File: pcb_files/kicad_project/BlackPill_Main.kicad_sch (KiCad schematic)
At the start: 32 parts, among them J10 Conn_01x04_Pin, J11 Conn_01x05_Pin, J9 Conn_01x04_Pin

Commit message: Actualiza el esquemático de la PCB
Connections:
- net BTN_MENU_MODE: now also U?.17 (B9); no longer U?.9 (A12)
- net BTN_START: now also U?.16 (B8); no longer U?.8 (A11)
- net LED_4: now also U?.24 (B10); no longer U?.5 (A8)
- net LED_5: now also U?.5 (A8); no longer U?.2 (B13)
- net LED_6: now also U?.26 (B1); no longer U?.1 (B12)
- net SPI_SCK: now also U?.2 (B13); no longer U?.24 (B10)
- net USART_RX renamed USART1_RX
- net USART_TX renamed USART1_TX
- new net SPI_NSS: U?.1 (B12)
- new net USART6_RX: U?.9 (A12)
- new net USART6_TX: U?.8 (A11)
- no-connect marks 14 -> 11
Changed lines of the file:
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@@
   (no_connect (at 80.01 185.42))
   (no_connect (at 97.79 81.28))
-  (no_connect (at 129.54 50.8))
   (no_connect (at 129.54 38.1))
   (no_connect (at 80.01 187.96))
   (no_connect (at 27.94 179.07))
-  (no_connect (at 97.79 76.2))
   (no_connect (at 80.01 168.91))
   (no_connect (at 129.54 53.34))
-  (no_connect (at 97.79 78.74))
   (no_connect (at 45.72 184.15))
   (no_connect (at 129.54 86.36))
@@
     (stroke (width 0) (type default))
   )
+  (wire (pts (xy 77.47 76.2) (xy 97.79 76.2))
+    (stroke (width 0) (type default))
+  )
   (wire (pts (xy 46.99 67.31) (xy 27.94 67.31))
     (stroke (width 0) (type default))
@@
     (stroke (width 0) (type default))
   )
-  (wire (pts (xy 144.78 48.26) (xy 129.54 48.26))
+  (wire (pts (xy 138.43 48.26) (xy 129.54 48.26))
     (stroke (width 0) (type default))
   )
@@
     (stroke (width 0) (type default))
   )
+  (wire (pts (xy 138.43 45.72) (xy 129.54 45.72))
+    (stroke (width 0) (type default))
+  )
   (wire (pts (xy 129.54 73.66) (xy 142.24 73.66))
     (stroke (width 0) (type default))
@@
     (stroke (width 0) (type default))
   )
-  (wire (pts (xy 81.28 38.1) (xy 97.79 38.1))
-    (stroke (width 0) (type default))
-  )
   (wire (pts (xy 270.51 107.95) (xy 267.97 107.95))
     (stroke (width 0) (type default))
@@
     (stroke (width 0) (type default))
   )
+  (wire (pts (xy 138.43 50.8) (xy 129.54 50.8))
+    (stroke (width 0) (type default))
+  )
   (wire (pts (xy 115.57 90.17) (xy 115.57 100.33))
     (stroke (width 0) (type default))
@@
     (stroke (width 0) (type default))
   )
-  (wire (pts (xy 153.67 40.64) (xy 129.54 40.64))
+  (wire (pts (xy 147.32 40.64) (xy 129.54 40.64))
     (stroke (width 0) (type default))
   )
@@
     (stroke (width 0) (type default))
   )
-  (wire (pts (xy 149.86 43.18) (xy 129.54 43.18))
-    (stroke (width 0) (type default))
-  )
-  (wire (pts (xy 81.28 55.88) (xy 97.79 55.88))
+  (wire (pts (xy 143.51 43.18) (xy 129.54 43.18))
     (stroke (width 0) (type default))
   )
@@
     (stroke (width 0) (type default))
   )
+  (wire (pts (xy 77.47 78.74) (xy 97.79 78.74))
+    (stroke (width 0) (type default))
+  )
   (wire (pts (xy 270.51 43.18) (xy 267.97 43.18))
     (stroke (width 0) (type default))
@@
     (stroke (width 0) (type default))
   )
-  (wire (pts (xy 81.28 40.64) (xy 97.79 40.64))
-    (stroke (width 0) (type default))
-  )
-  (wire (pts (xy 81.28 58.42) (xy 97.79 58.42))
-    (stroke (width 0) (type default))
+  (label "BTN_MENU_MODE" (at 77.47 78.74 0) (fields_autoplaced)
+    (effects (font (size 1.27 1.27)) (justify left bottom))
   )
   (label "LED_4" (at 254 82.55 0) (fields_autoplaced)
@@
     (effects (font (size 1.27 1.27)) (justify left bottom))
   )
-  (label "LED_3" (at 144.78 48.26 180) (fields_autoplaced)
+  (label "LED_3" (at 138.43 48.26 180) (fields_autoplaced)
     (effects (font (size 1.27 1.27)) (justify right bottom))
   )
@@
     (effects (font (size 1.27 1.27)) (justify right bottom))
   )
-  (label "USART_TX" (at 81.28 50.8 0) (fields_autoplaced)
+  (label "USART1_TX" (at 81.28 50.8 0) (fields_autoplaced)
     (effects (font (size 1.27 1.27)) (justify left bottom))
   )
@@
     (effects (font (size 1.524 1.524)) (justify left bottom))
   )
-  (label "BTN_START" (at 81.28 55.88 0) (fields_autoplaced)
+  (label "BTN_START" (at 77.47 76.2 0) (fields_autoplaced)
     (effects (font (size 1.27 1.27)) (justify left bottom))
   )
@@
     (effects (font (size 1.27 1.27)) (justify left bottom))
   )
+  (label "LED_6" (at 138.43 50.8 180) (fields_autoplaced)
+    (effects (font (size 1.27 1.27)) (justify right bottom))
+  )
   (label "SWCLK" (at 115.57 100.33 90) (fields_autoplaced)
     (effects (font (size 1.524 1.524)) (justify left bottom))
@@
     (effects (font (size 1.27 1.27)) (justify right bottom))
   )
-  (label "USART_RX" (at 128.27 113.03 0) (fields_autoplaced)
+  (label "USART1_RX" (at 128.27 113.03 0) (fields_autoplaced)
     (effects (font (size 1.27 1.27)) (justify left bottom))
   )
-  (label "LED_6" (at 81.28 38.1 0) (fields_autoplaced)
+  (label "USART1_TX" (at 128.27 110.49 0) (fields_autoplaced)
     (effects (font (size 1.27 1.27)) (justify left bottom))
   )
-  (label "USART_TX" (at 128.27 110.49 0) (fields_autoplaced)
+  (label "USART1_RX" (at 81.28 53.34 0) (fields_autoplaced)
     (effects (font (size 1.27 1.27)) (justify left bottom))
   )
-  (label "USART_RX" (at 81.28 53.34 0) (fields_autoplaced)
-    (effects (font (size 1.27 1.27)) (justify left bottom))
-  )
   (label "SENSOR_1" (at 142.24 73.66 180) (fields_autoplaced)
     (effects (font (size 1.27 1.27)) (justify right bottom))
@@
   )
   (label "BTN_MENU_MODE" (at 240.03 52.07 180) (fields_autoplaced)
+    (effects (font (size 1.27 1.27)) (justify right bottom))
+  )
+  (label "LED_4" (at 138.43 45.72 180) (fields_autoplaced)
     (effects (font (size 1.27 1.27)) (justify right bottom))
   )
@@
     (effects (font (size 1.27 1.27)) (justify right bottom))
   )
-  (label "LED_5" (at 81.28 40.64 0) (fields_autoplaced)
-    (effects (font (size 1.27 1.27)) (justify left bottom))
-  )
   (label "SENSOR_3" (at 142.24 68.58 180) (fields_autoplaced)
     (effects (font (size 1.27 1.27)) (justify right bottom))
-  )
-  (label "BTN_MENU_MODE" (at 81.28 58.42 0) (fields_autoplaced)
-    (effects (font (size 1.27 1.27)) (justify left bottom))
   )
   (label "LED_2" (at 254 55.88 0) (fields_autoplaced)
@@
     (effects (font (size 1.27 1.27)) (justify right bottom))
   )
-  (label "LED_4" (at 81.28 48.26 0) (fields_autoplaced)
+  (label "LED_5" (at 81.28 48.26 0) (fields_autoplaced)
     (effects (font (size 1.27 1.27)) (justify left bottom))
   )
@@
     (effects (font (size 1.27 1.27)) (justify right))
   )
+  (hierarchical_label "SPI_SCK" (shape bidirectional) (at 97.79 40.64 180) (fields_autoplaced)
+    (effects (font (size 1.27 1.27)) (justify right))
+  )
   (hierarchical_label "ENC_2_I" (shape input) (at 97.79 60.96 180) (fields_autoplaced)
     (effects (font (size 1.27 1.27)) (justify right))
@@
     (effects (font (size 1.27 1.27)) (justify right))
   )
+  (hierarchical_label "USART6_TX" (shape input) (at 97.79 55.88 180) (fields_autoplaced)
+    (effects (font (size 1.27 1.27)) (justify right))
+  )
   (hierarchical_label "ENC_2_B" (shape input) (at 97.79 66.04 180) (fields_autoplaced)
     (effects (font (size 1.27 1.27)) (justify right))
@@
     (effects (font (size 1.27 1.27)) (justify right))
   )
+  (hierarchical_label "SPI_NSS" (shape bidirectional) (at 97.79 38.1 180) (fields_autoplaced)
+    (effects (font (size 1.27 1.27)) (justify right))
+  )
   (hierarchical_label "ENC_1_A" (shape input) (at 97.79 73.66 180) (fields_autoplaced)
     (effects (font (size 1.27 1.27)) (justify right))
   )
-  (hierarchical_label "SPI_SCK" (shape bidirectional) (at 129.54 45.72 0) (fields_autoplaced)
-    (effects (font (size 1.27 1.27)) (justify left))
+  (hierarchical_label "USART6_RX" (shape input) (at 97.79 58.42 180) (fields_autoplaced)
+    (effects (font (size 1.27 1.27)) (justify right))
   )
   (hierarchical_label "SPI_MOSI" (shape bidirectional) (at 97.79 45.72 180) (fields_autoplaced)
@@
     )
   )
-  (symbol (lib_id "power:+3V3") (at 149.86 43.18 180) (unit 1)
-    (in_bom yes) (on_board yes) (dnp no) (fields_autoplaced)
-    (property "Reference" "#PWR030" (at 149.86 39.37 0)
-      (effects (font (size 1.27 1.27)) hide)
-    )
-    (property "Value" "+3V3" (at 149.86 48.26 0)
-      (effects (font (size 1.27 1.27)))
-    )
-    (property "Footprint" "" (at 149.86 43.18 0)
-      (effects (font (size 1.27 1.27)) hide)
-    )
-    (property "Datasheet" "" (at 149.86 43.18 0)
+  (symbol (lib_id "power:+3V3") (at 143.51 43.18 180) (unit 1)
+    (in_bom yes) (on_board yes) (dnp no) (fields_autoplaced)
+    (property "Reference" "#PWR030" (at 143.51 39.37 0)
+      (effects (font (size 1.27 1.27)) hide)
+    )
+    (property "Value" "+3V3" (at 143.51 48.26 0)
+      (effects (font (size 1.27 1.27)))
+    )
+    (property "Footprint" "" (at 143.51 43.18 0)
+      (effects (font (size 1.27 1.27)) hide)
+    )
+    (property "Datasheet" "" (at 143.51 43.18 0)
       (effects (font (size 1.27 1.27)) hide)
     )
@@
     )
   )
-  (symbol (lib_id "power:GND") (at 153.67 40.64 0) (unit 1)
-    (in_bom yes) (on_board yes) (dnp no)
-    (property "Reference" "#PWR031" (at 153.67 46.99 0)
-      (effects (font (size 1.27 1.27)) hide)
-    )
-    (property "Value" "GND" (at 153.67 44.45 0)
-      (effects (font (size 1.27 1.27)))
-    )
-    (property "Footprint" "" (at 153.67 40.64 0)
-      (effects (font (size 1.27 1.27)) hide)
-    )
-    (property "Datasheet" "" (at 153.67 40.64 0)
-      (effects (font (size 1.27 1.27)) hide)
-    )
+  (symbol (lib_id "power:GND") (at 147.32 40.64 0) (unit 1)
+    (in_bom yes) (on_board yes) (dnp no)
+    (property "Reference" "#PWR031" (at 147.32 46.99 0)
+      (effects (font (size 1.27 1.27)) hide)
+    )
+    (property "Value" "GND" (at 147.32 44.45 0)
+      (effects (font (size 1.27 1.27)))
+    )
+    (property "Footprint" "" (at 147.32 40.64 0)
+      (effects (font (size 1.27 1.27)) hide)
+    )
+    (property "Datasheet" "" (at 147.32 40.64 0)
+      (effects (font (size 1.27 1.27)) hide)
+    )

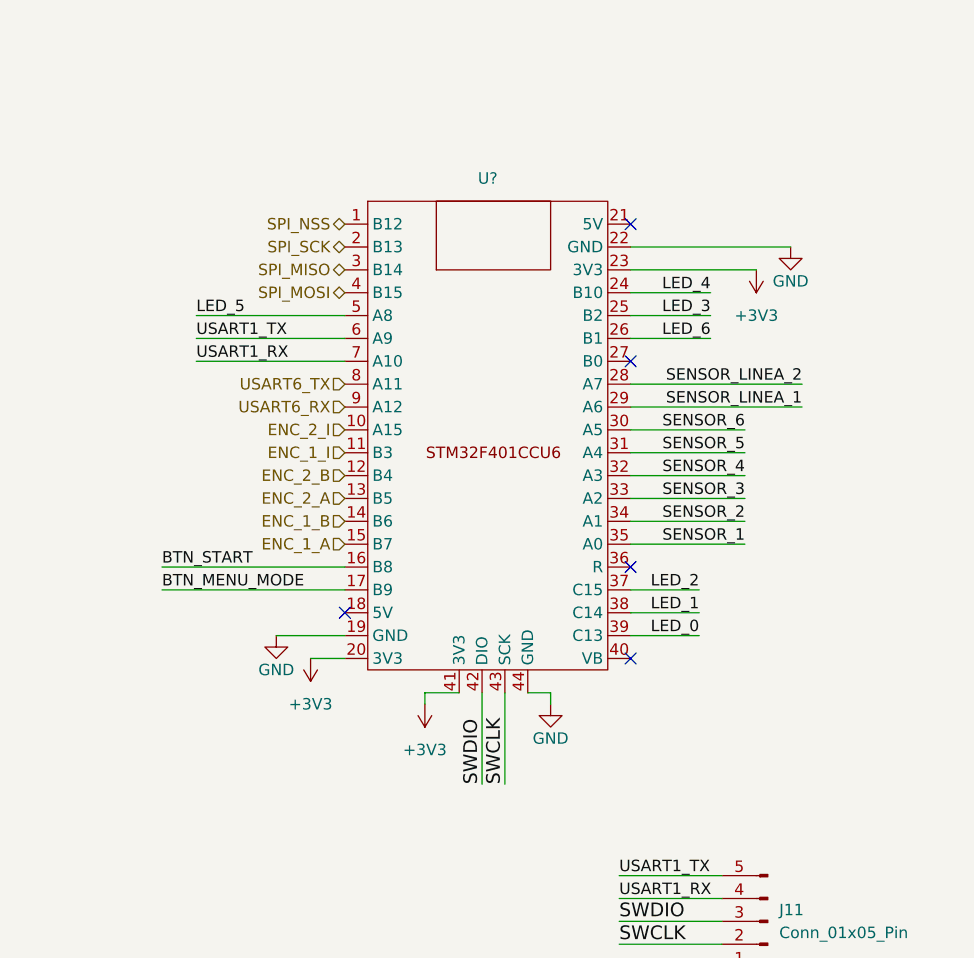
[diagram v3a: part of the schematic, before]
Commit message: Actualiza esquemático e inicia PCB
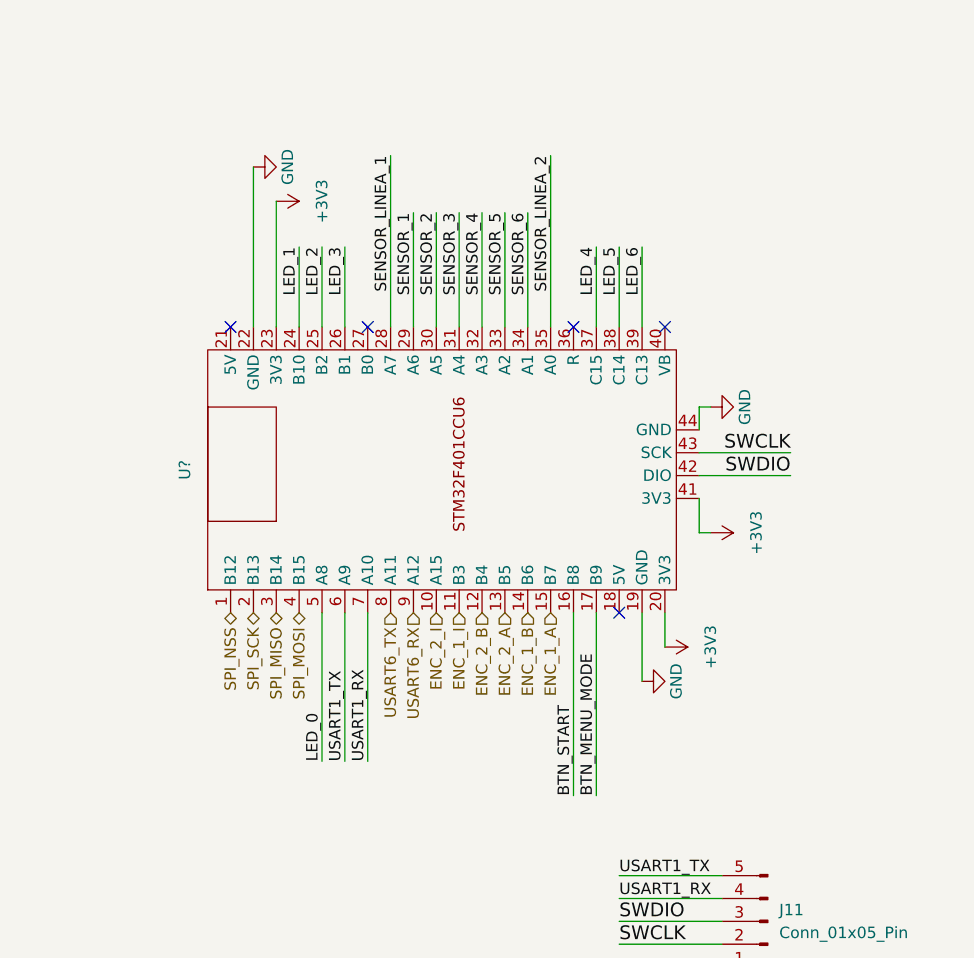
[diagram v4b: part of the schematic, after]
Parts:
- STEP?: footprint custom_symbols:Mini360 -> custom_footprints:Mini360
- SW1: footprint custom_symbols:Switch6P -> custom_footprints:Switch6P
- U?: footprint custom_symbols:BlackPill_STM32F401 -> custom_footprints:BlackPill_STM32F401
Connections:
- net LED_0: now also U?.5 (A8); no longer U?.39 (C13)
- net LED_1: now also U?.24 (B10); no longer U?.38 (C14)
- net LED_2: now also U?.25 (B2); no longer U?.37 (C15)
- net LED_3: now also U?.26 (B1); no longer U?.25 (B2)
- net LED_4: now also U?.37 (C15); no longer U?.24 (B10)
- net LED_5: now also U?.38 (C14); no longer U?.5 (A8)
- net LED_6: now also U?.39 (C13); no longer U?.26 (B1)
- net SENSOR_1: now also U?.29 (A6); no longer U?.35 (A0)
- net SENSOR_2: now also U?.30 (A5); no longer U?.34 (A1)
- net SENSOR_3: now also U?.31 (A4); no longer U?.33 (A2)
- net SENSOR_5: now also U?.33 (A2); no longer U?.31 (A4)
- net SENSOR_6: now also U?.34 (A1); no longer U?.30 (A5)
- net SENSOR_LINEA_1: now also U?.28 (A7); no longer U?.29 (A6)
- net SENSOR_LINEA_2: now also U?.35 (A0); no longer U?.28 (A7)
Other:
- moved on the sheet: U?

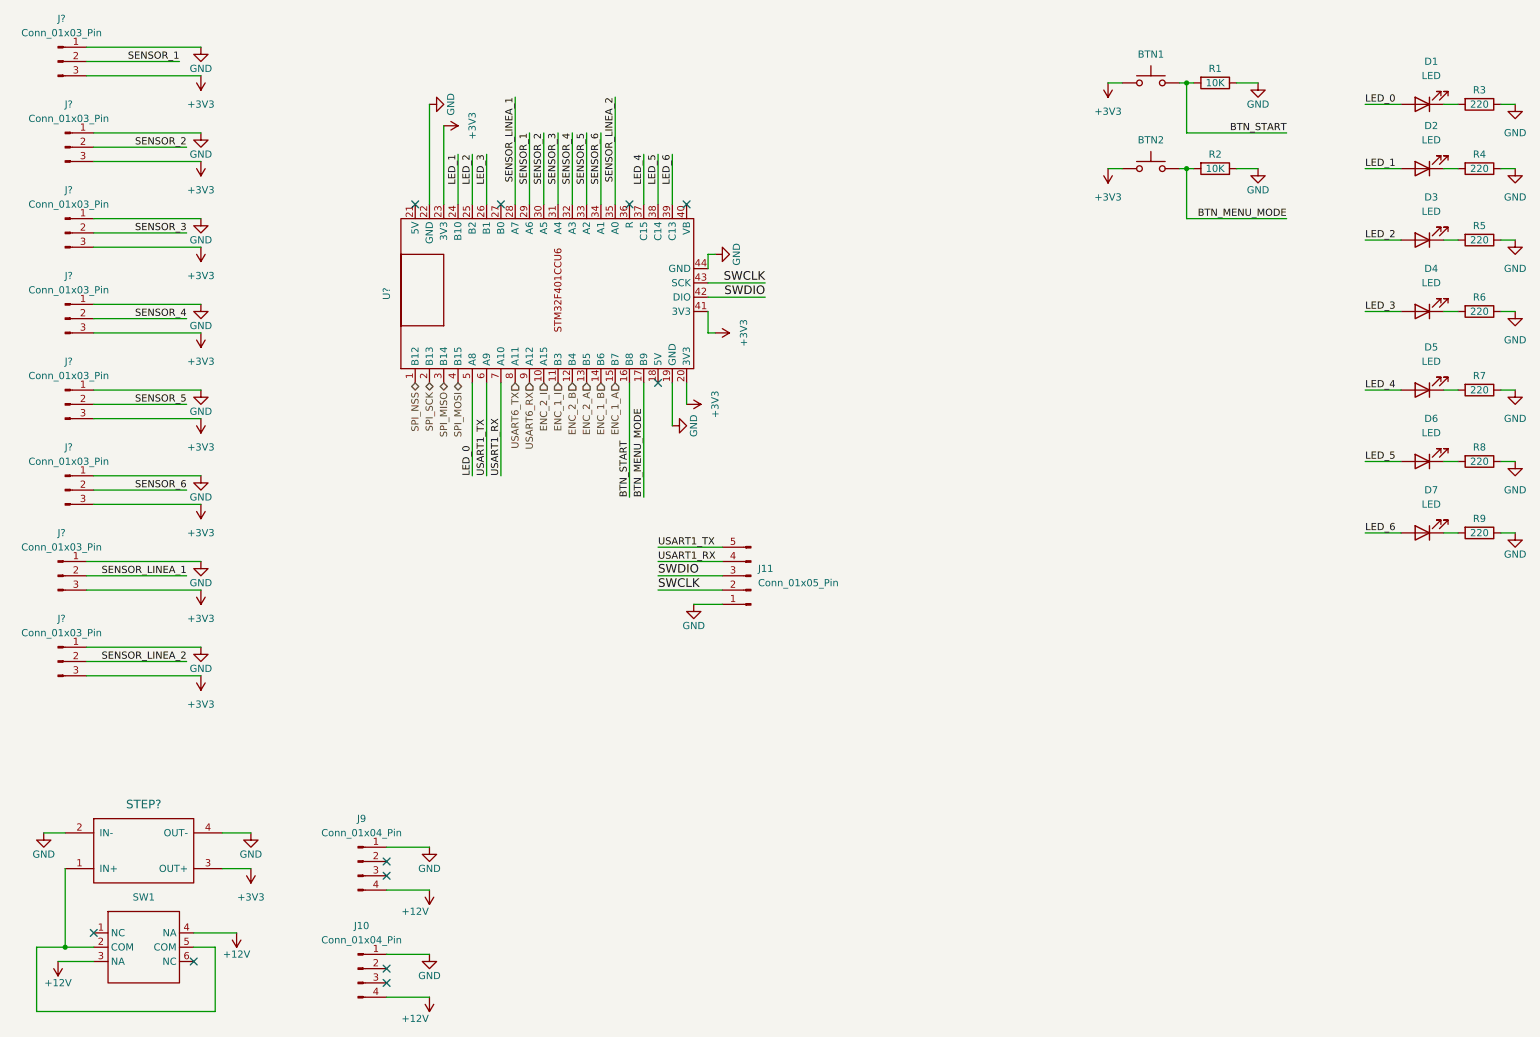
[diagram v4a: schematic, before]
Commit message: Actualiza esquemático y finaliza ruteado de PCB
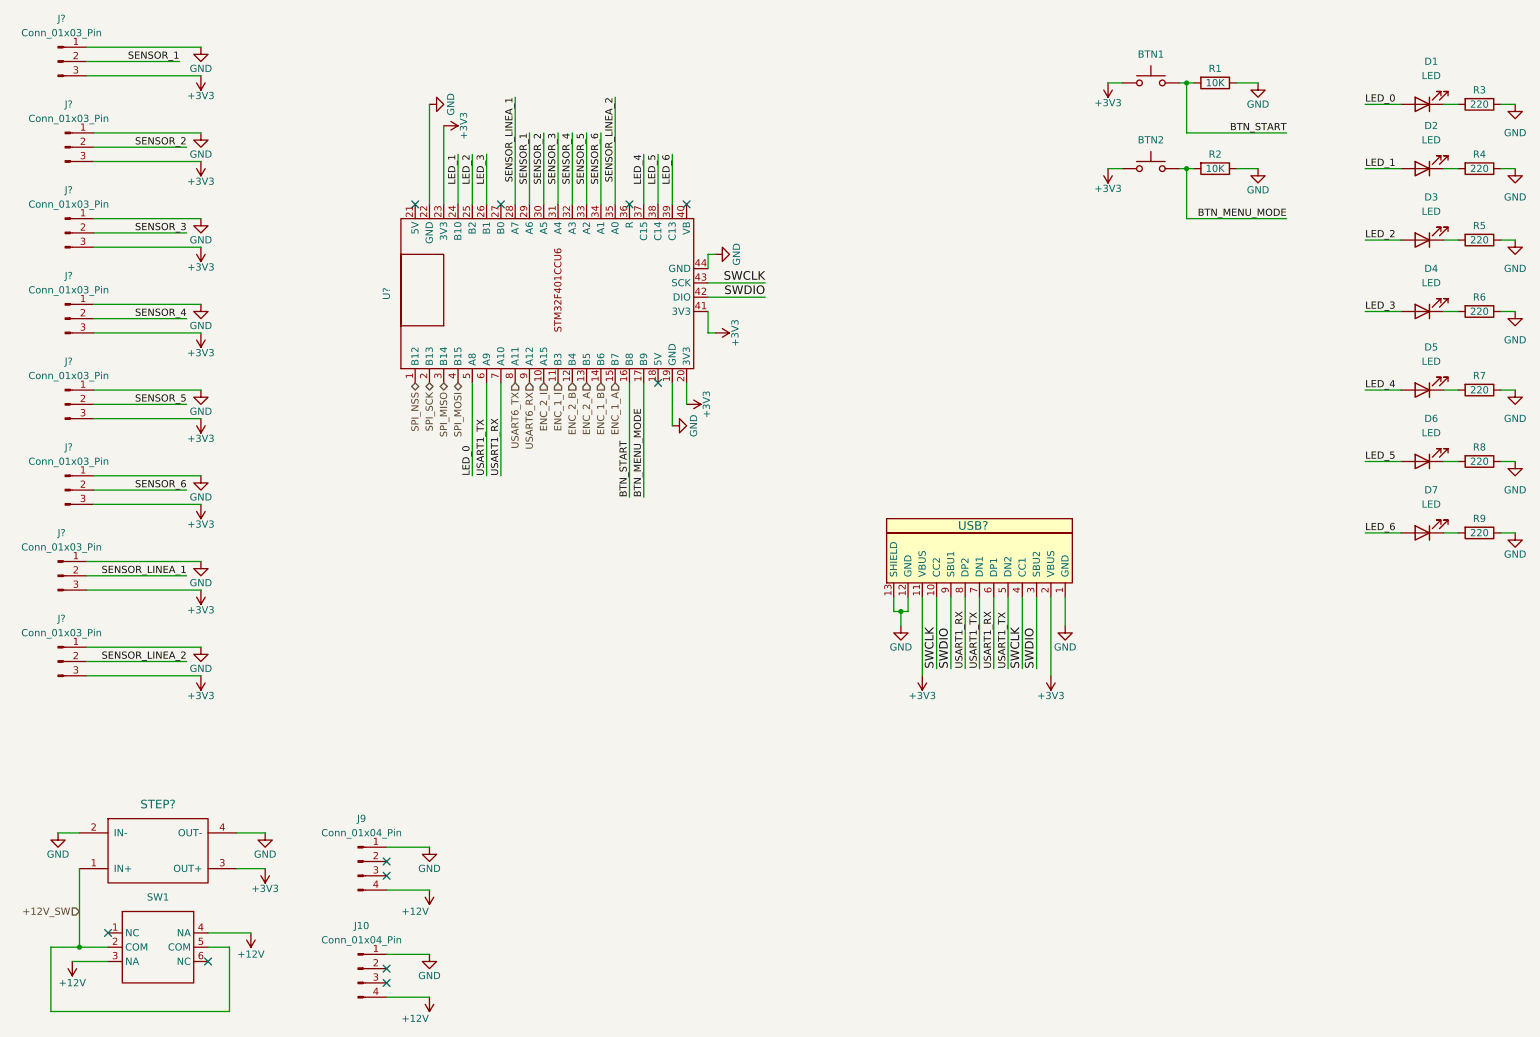
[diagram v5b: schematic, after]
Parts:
- removed J11: Conn_01x05_Pin, Connector_PinHeader_2.54mm:PinHeader_1x05_P2.54mm_Vertical, symbol Connector:Conn_01x05_Pin
- added USB?: ~, custom_footprints:USB-C ST-Link USART, symbol custom_symbols:USB-C_ST-Link_USART
- J10, J9: footprint Connector_PinHeader_2.54mm:PinHeader_1x04_P2.54mm_Vertical -> Connector_JST:JST_XH_B4B-XH-AM_1x04_P2.50mm_Vertical
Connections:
- net +3V3: now also USB?.11 (VBUS), USB?.2 (VBUS)
- net GND: now also USB?.1 (GND), USB?.12 (GND), USB?.13 (SHIELD)
- net SWCLK: now also USB?.10 (CC2), USB?.4 (CC1)
- net SWDIO: now also USB?.3 (SBU2), USB?.9 (SBU1)
- net USART1_RX: now also USB?.6 (DP1), USB?.8 (DP2)
- net USART1_TX: now also USB?.5 (DN2), USB?.7 (DN1)
- net +12V_SW: now reaches STEP?.1 (IN+), SW1.2 (COM), SW1.5 (COM)
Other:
- moved on the sheet: STEP?, SW1
